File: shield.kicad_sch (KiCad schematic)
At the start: 0 parts

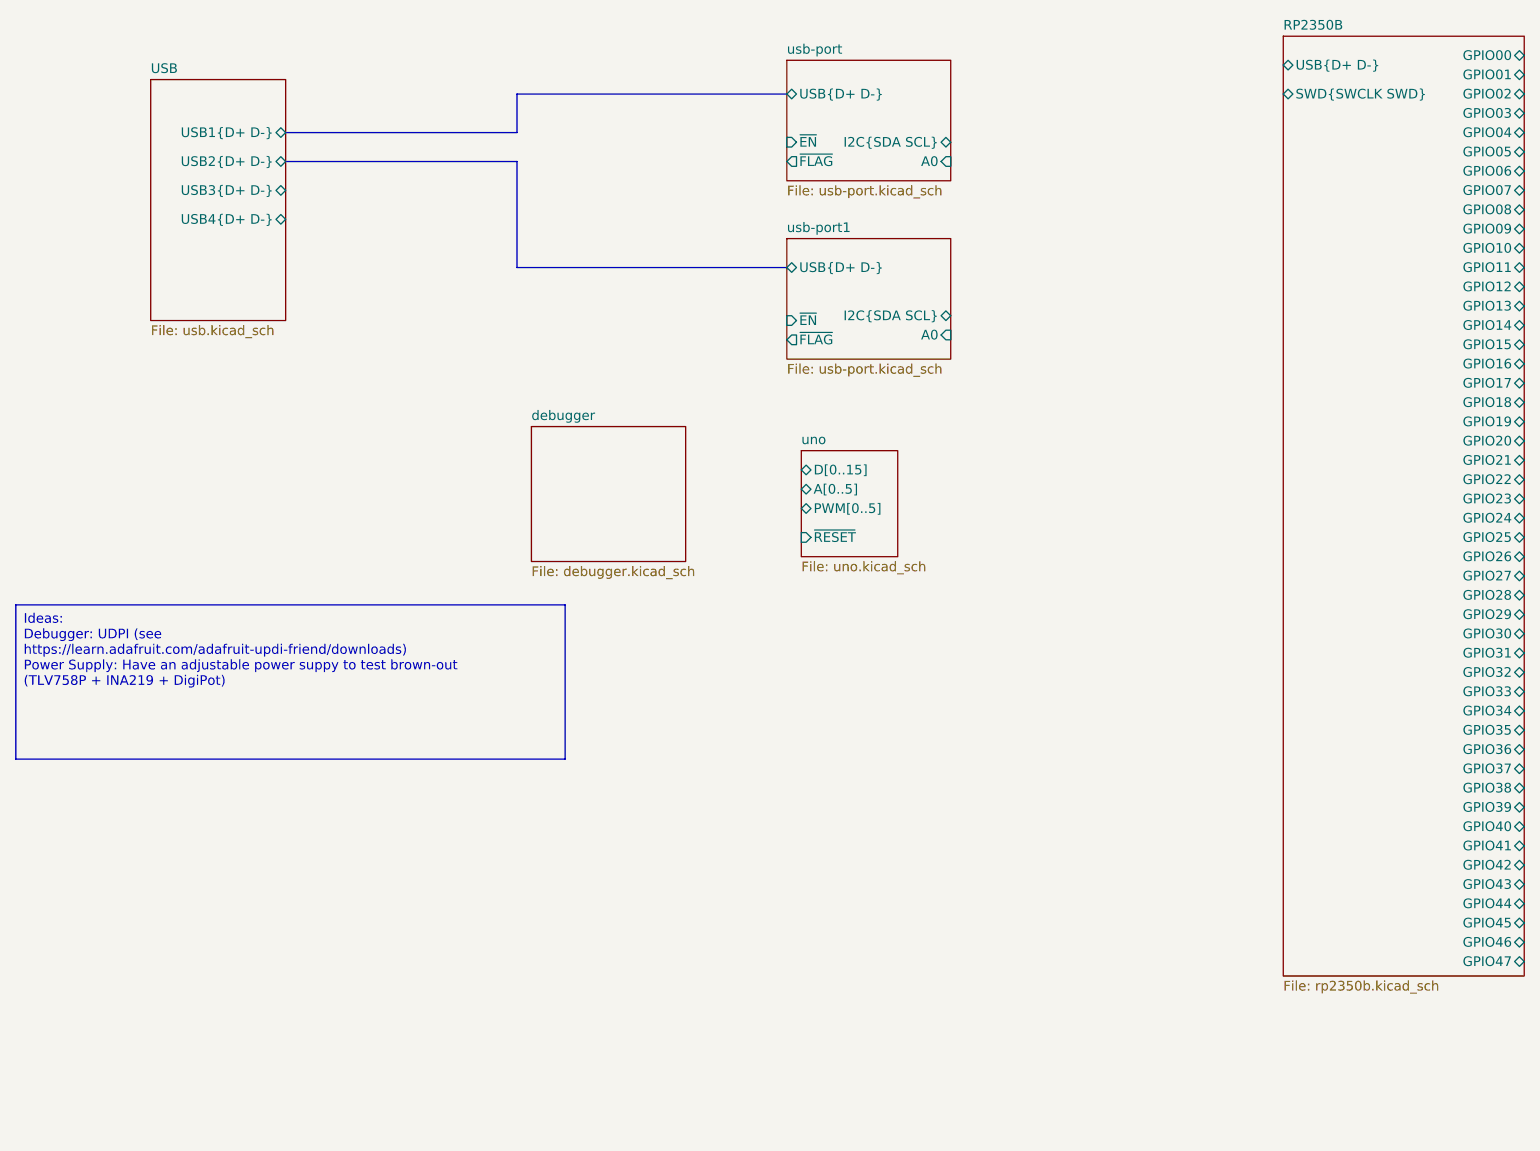
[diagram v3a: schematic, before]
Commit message: Do pin assignment for tester
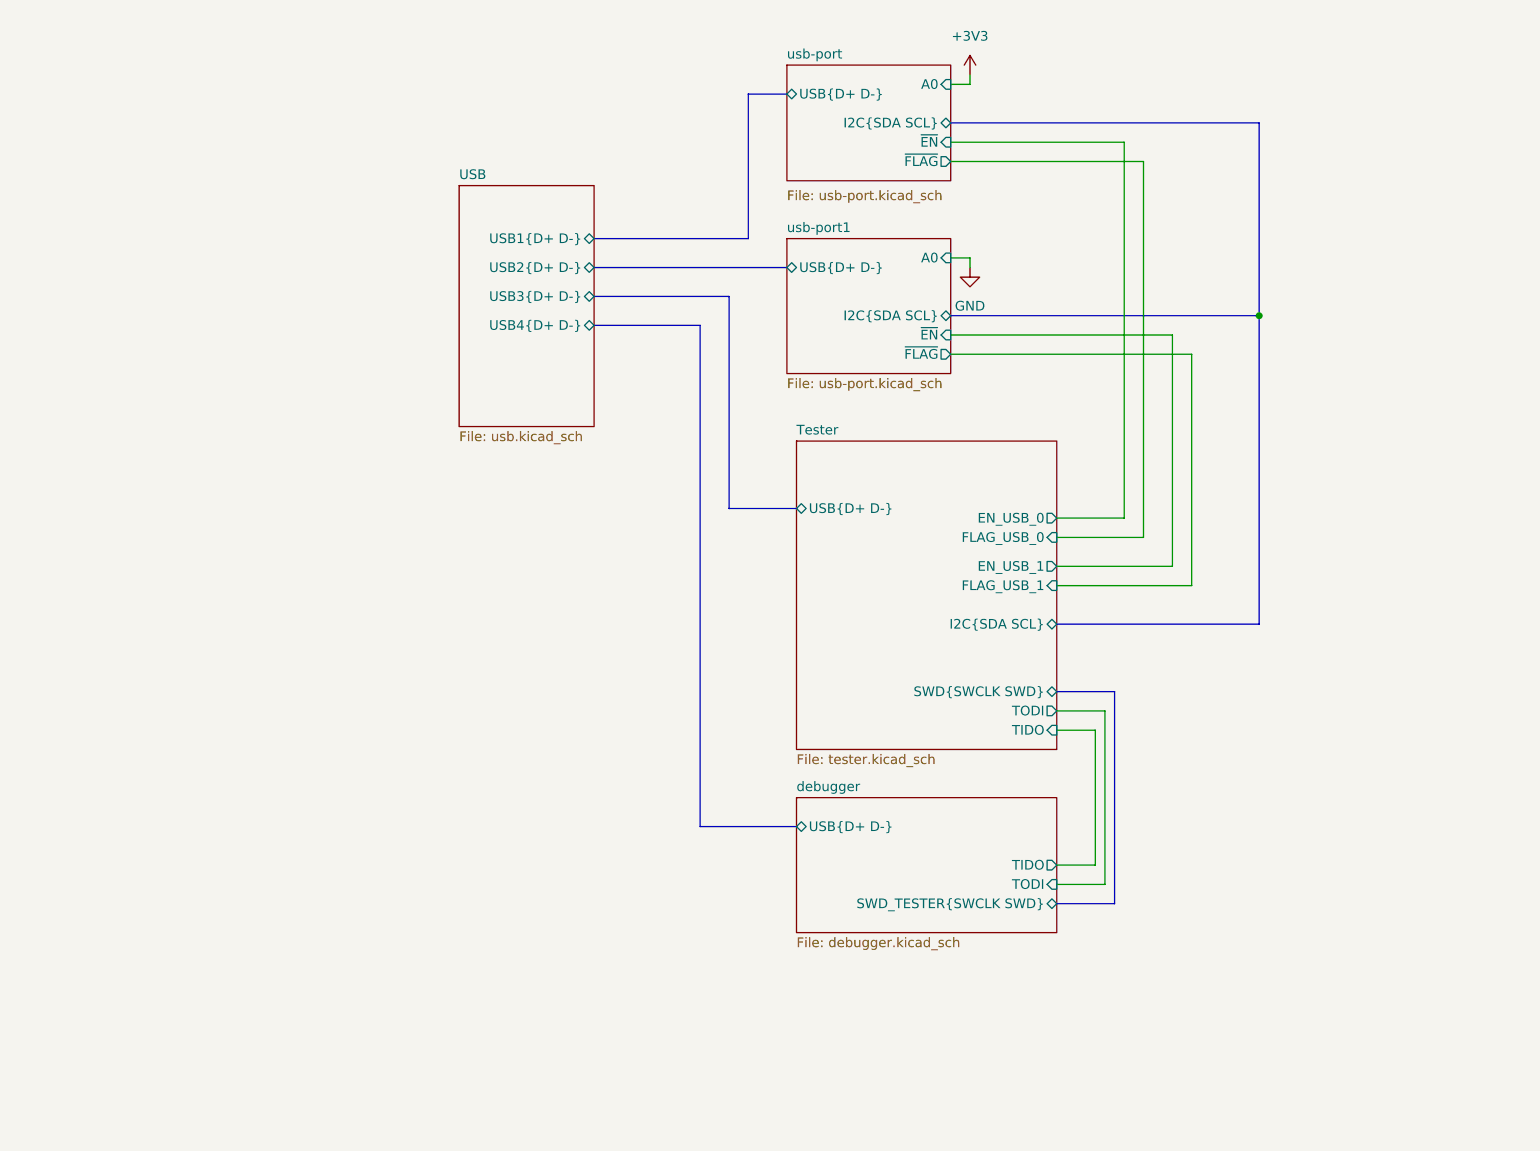
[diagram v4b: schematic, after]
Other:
- removed sheet RP2350B
- removed sheet uno
- added sheet Tester (tester.kicad_sch)
- sheet debugger ports: added SWD_TESTER{SWCLK SWD}, TIDO, TODI, USB{D+ D-}; removed none

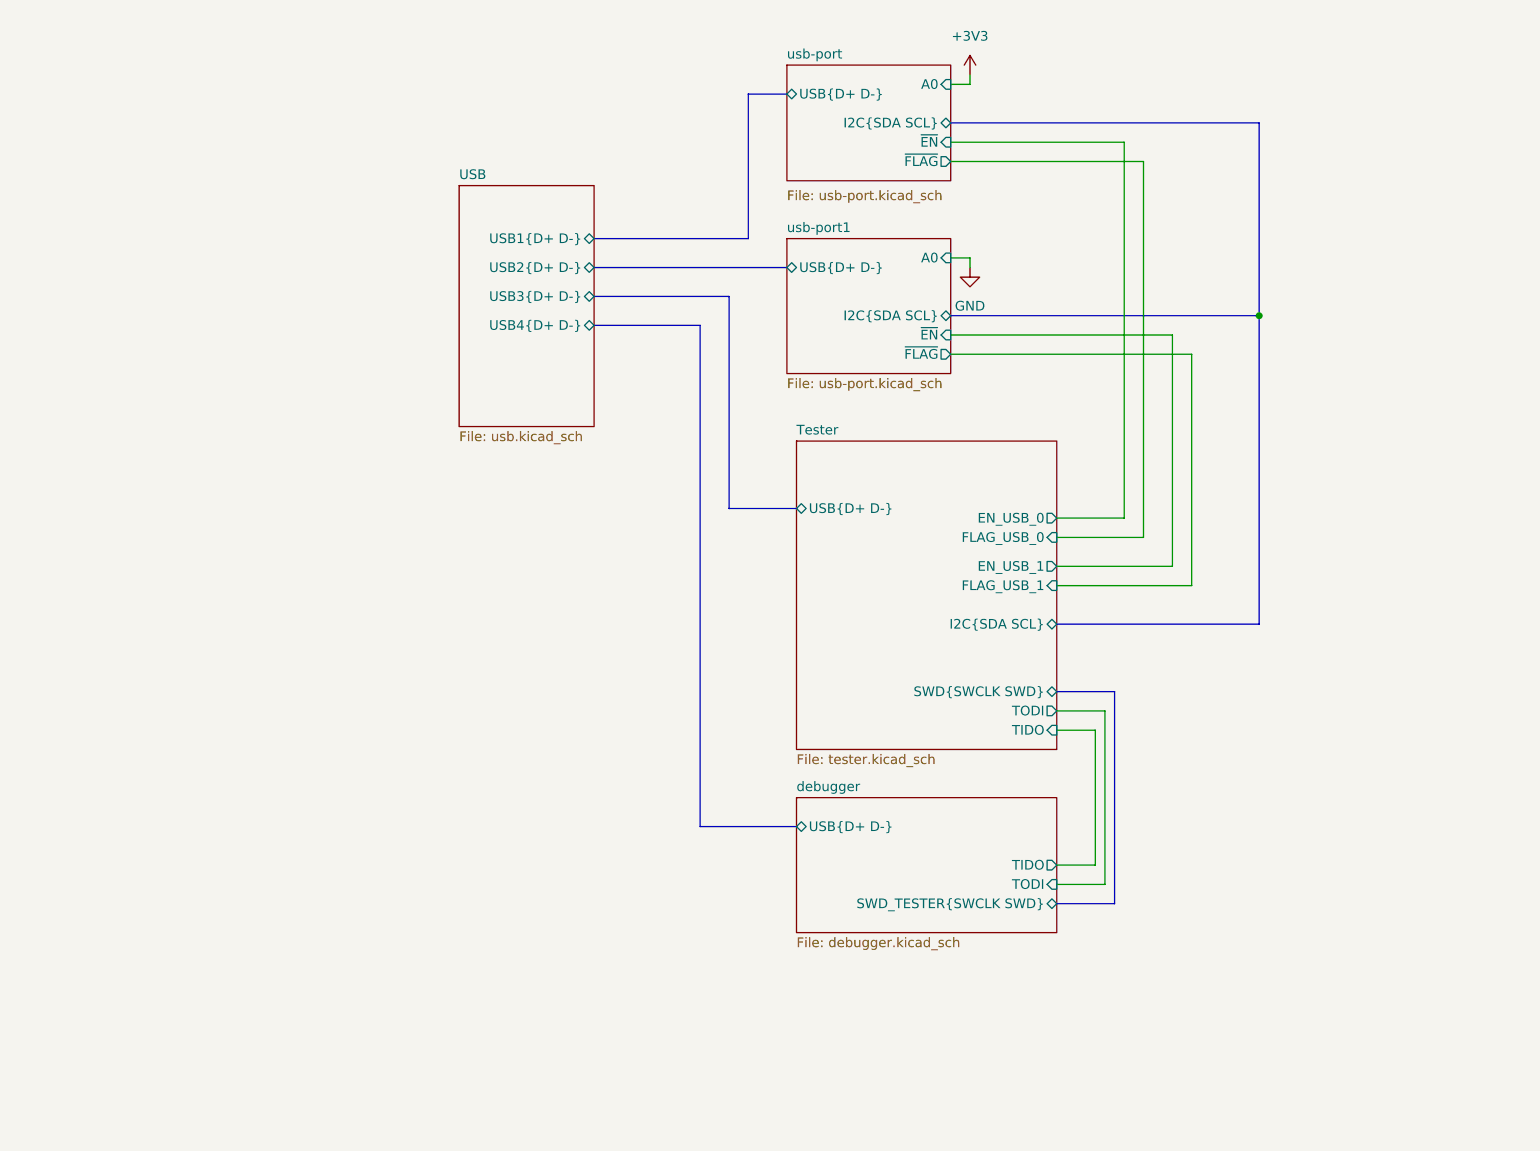
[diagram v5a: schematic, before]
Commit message: Fix rev1 errors
Add USB mux to allow for USB PIO
Fix D+ D- mixup
Fix USB Hub LED indicator label
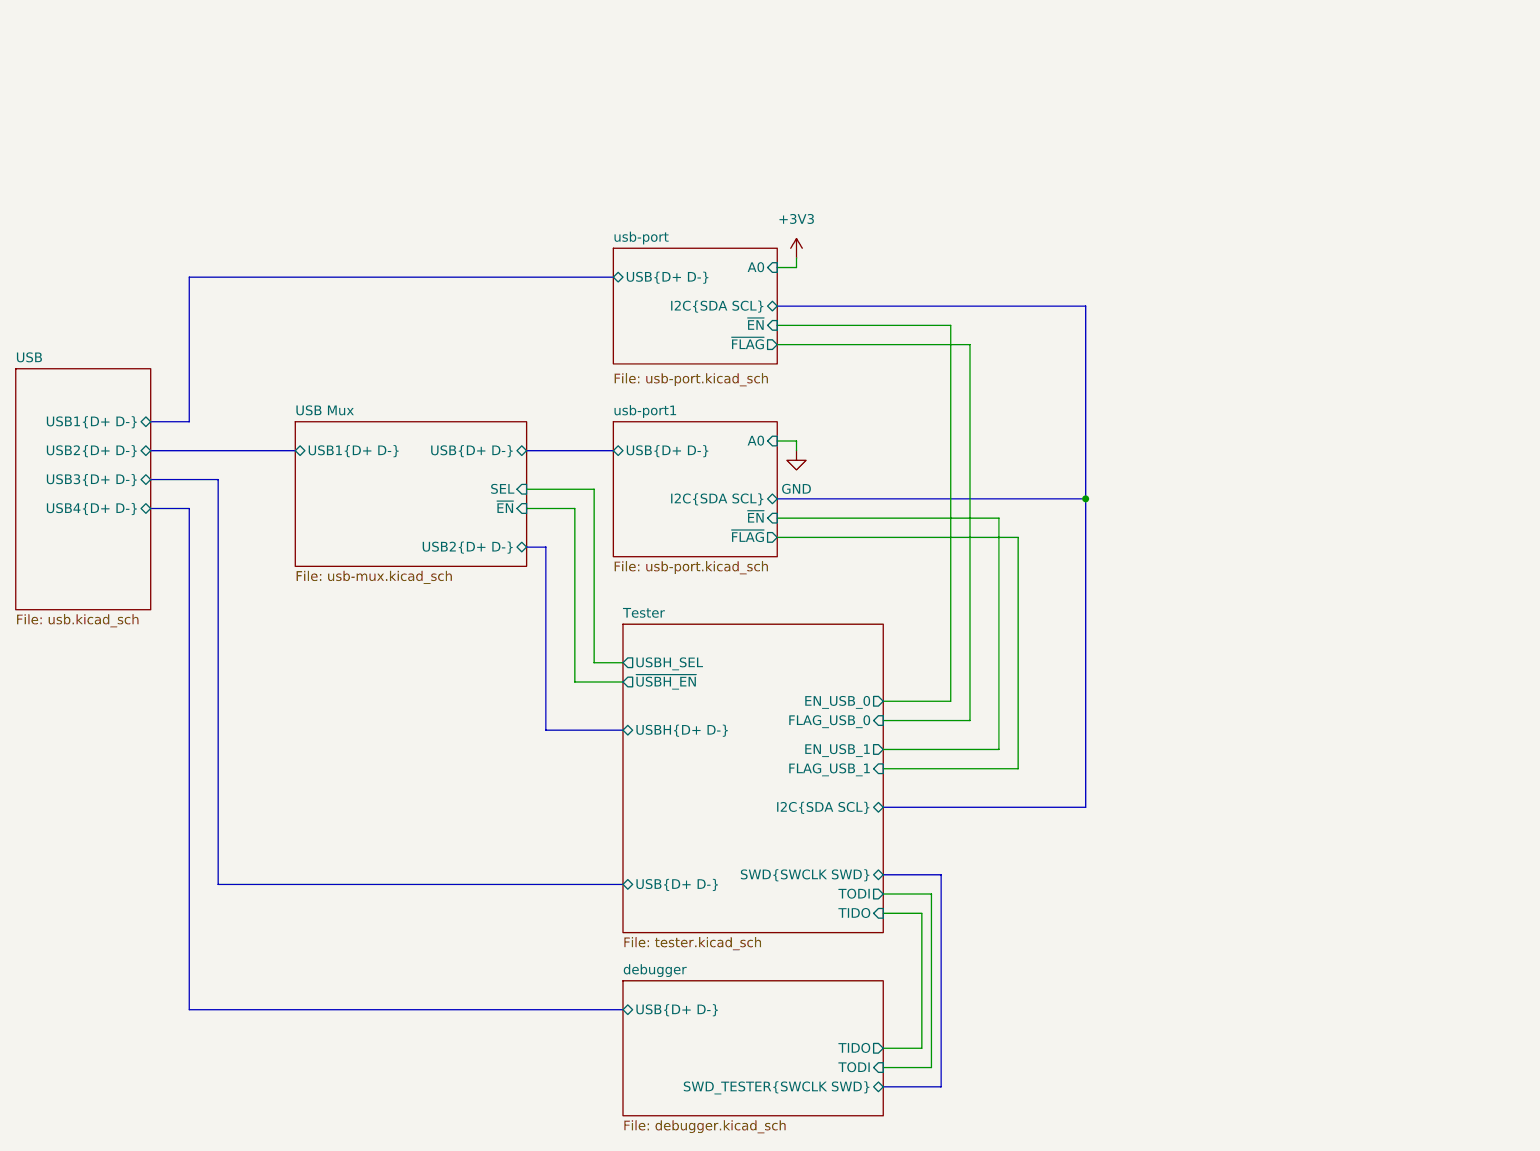
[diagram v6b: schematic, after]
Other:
- added sheet USB Mux (usb-mux.kicad_sch)
- sheet Tester ports: added USBH_SEL, USBH{D+ D-}, ~{USBH_EN}; removed none
